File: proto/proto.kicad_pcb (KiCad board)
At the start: 2 copper layers, 76.2 x 50.8 mm, 307 parts, among them J1 STM32WORLD_CONNECTOR_2, J2 STM32WORLD_CONNECTOR_1, J3 STM32WORLD_BOARD

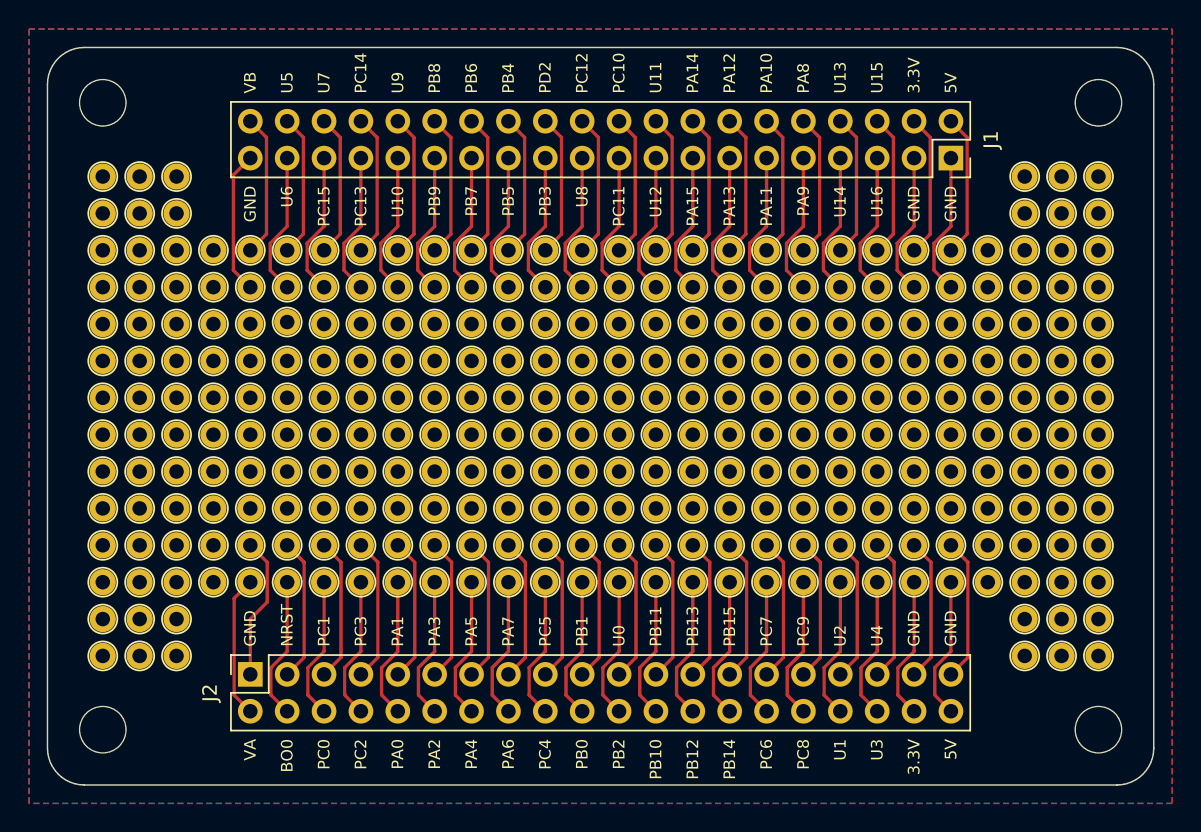
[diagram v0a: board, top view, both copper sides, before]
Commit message: mem24cxx ready
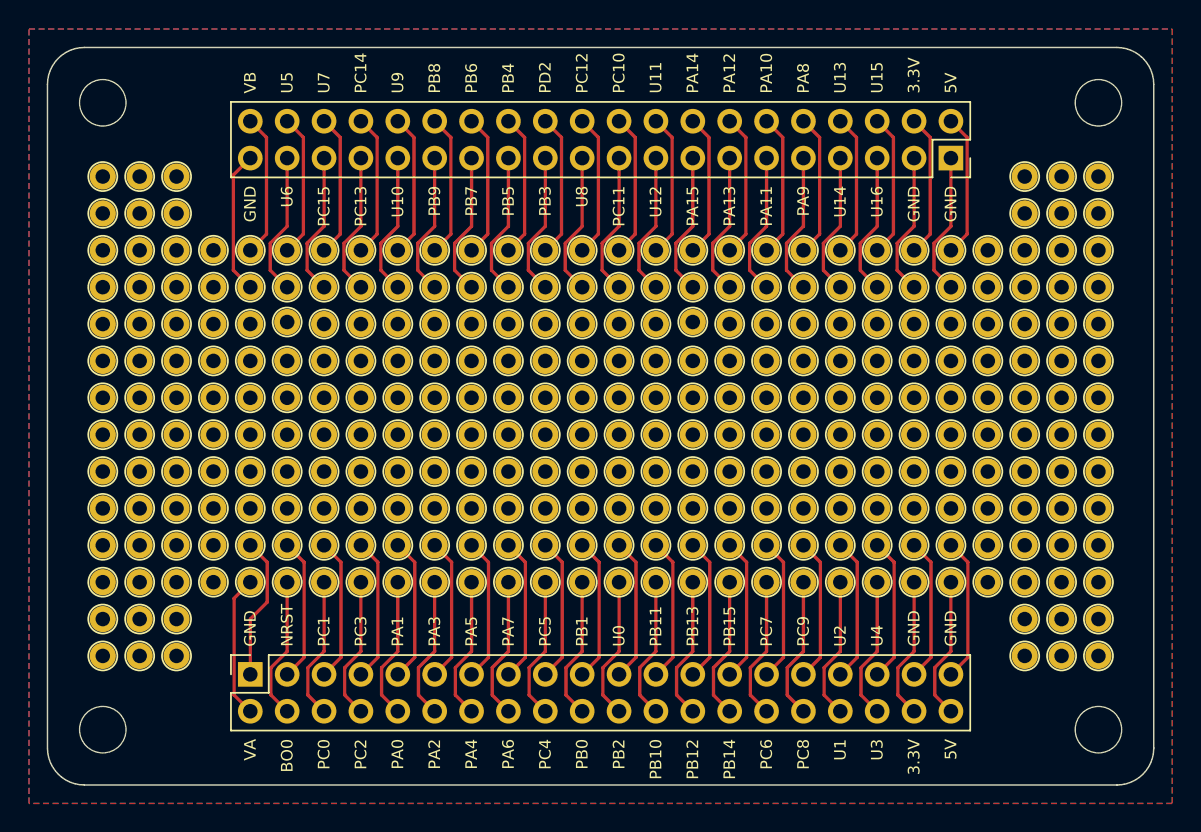
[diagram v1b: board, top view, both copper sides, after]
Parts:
- renumbered J2 to J1, J1 to J2
